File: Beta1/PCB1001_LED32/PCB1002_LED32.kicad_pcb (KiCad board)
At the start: 2 copper layers, 194 x 15.5 mm, 227 parts, among them U0 APA102C, U1 APA102C, U10 APA102C, U11 APA102C, U12 APA102C, U13 APA102C, U14 APA102C, U15 APA102C, U16 APA102C, U17 APA102C, U18 APA102C, U19 APA102C, U2 APA102C, U20 APA102C, U21 APA102C, U22 APA102C, U23 APA102C, U24 APA102C, U25 APA102C, U26 APA102C, U27 APA102C, U28 APA102C, U29 APA102C, U3 APA102C, U30 APA102C, U31 APA102C, U4 APA102C, U5 APA102C, U6 APA102C, U7 APA102C, U8 APA102C, U9 APA102C

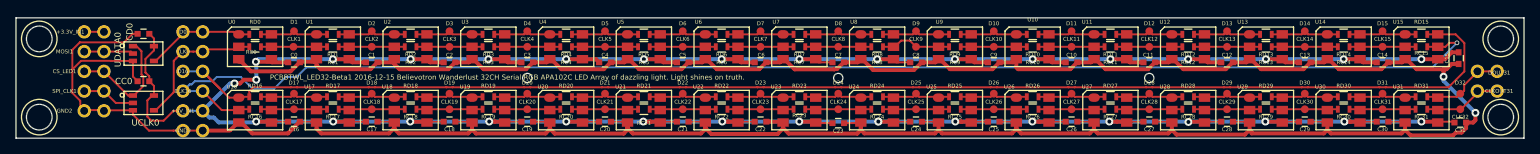
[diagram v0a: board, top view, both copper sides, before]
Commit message: Reduced width by 5.08, equally L/R
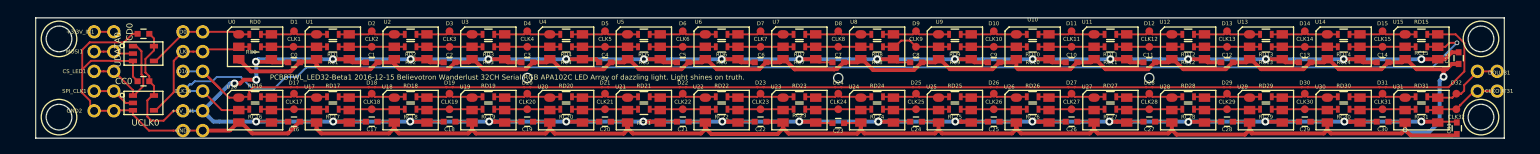
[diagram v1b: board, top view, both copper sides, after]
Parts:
- moved REF** 2.54 mm to (188.4, -12.8)
- moved REF** 2.54 mm to (188.4, -2.71)
- moved REF** 2.54 mm to (5.54, -12.8)
- moved REF** 2.54 mm to (5.54, -2.71)
- moved +3.3V_IN1 1.27 mm to (10.1, -13.7)
- moved CS_LED1 1.27 mm to (10.1, -8.60)
- moved GND2 1.27 mm to (10.1, -3.52)
- moved MOSI1 1.27 mm to (10.1, -11.1)
- moved SPI_CLK1 1.27 mm to (10.1, -6.06)
- moved +3.3V_INB1 1.27 mm to (12.6, -13.7)
- moved CS_LEDB1 1.27 mm to (12.6, -8.60)
- moved GNDB2 1.27 mm to (12.6, -3.52)
- moved MOSIB1 1.27 mm to (12.6, -11.1)
- moved SPI_CLKB1 1.27 mm to (12.6, -6.06)
- moved C31 0.87 mm to (185.3, -1.27), turned to 270 degrees
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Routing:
- net GND: track 456.4 -> 453.0 mm
- net Net-(SPI_CLK1-Pad1): track 6.90 -> 5.63 mm
- net Net-(MOSI1-Pad1): track 6.38 -> 5.11 mm
- net Net-(CS_LED1-Pad1): track 15.4 -> 14.5 mm
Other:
- board size 194 x 15.5 mm -> 188.9 x 15.5 mm

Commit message: Removed jumper resistors, b/c as they cause shorts.
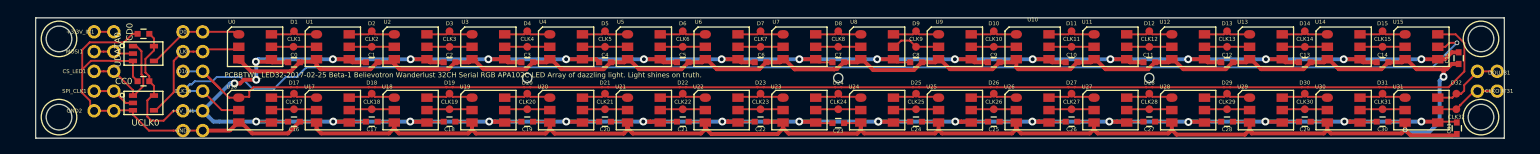
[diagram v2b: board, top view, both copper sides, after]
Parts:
- removed RC0, RC1, RC10, RC11, RC12, RC13, RC14, RC15, RC16, RC17, RC18, RC19, RC2, RC20, RC21, RC22, RC23, RC24, RC25, RC26, RC27, RC28, RC29, RC3, RC30, RC31, RC4, RC5, RC6, RC7, RC8, RC9, RD0, RD1, RD10, RD11, RD12, RD13, RD14, RD15, RD16, RD17, RD18, RD19, RD2, RD20, RD21, RD22, RD23, RD24, RD25, RD26, RD27, RD28, RD29, RD3, RD30, RD31, RD4, RD5, RD6, RD7, RD8, RD9: ZERO, Resistors_SMD:R_0603
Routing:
- net /CLK16: track 181.2 -> 178.5 mm
- net Net-(D31-Pad1): track 8.83 -> 6.13 mm
- net Net-(D30-Pad1): track 8.83 -> 6.13 mm
- net Net-(D29-Pad1): track 8.83 -> 6.13 mm
- net Net-(D28-Pad1): track 8.83 -> 6.13 mm
- net Net-(D27-Pad1): track 8.83 -> 6.13 mm
- net Net-(D15-Pad1): track 8.83 -> 6.13 mm
- net Net-(D14-Pad1): track 8.83 -> 6.13 mm
- net Net-(D13-Pad1): track 8.83 -> 6.13 mm
- net Net-(D11-Pad1): track 8.83 -> 6.13 mm
- net Net-(CLK31-Pad1): track 8.50 -> 5.80 mm
- net Net-(CLK30-Pad1): track 8.50 -> 5.80 mm
- net Net-(CLK29-Pad1): track 8.50 -> 5.80 mm
- net Net-(CLK28-Pad1): track 8.50 -> 5.80 mm
- net Net-(CLK27-Pad1): track 8.50 -> 5.80 mm
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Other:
- board text added: "PCBBTWL_LED32-2017-02-25 Beta-1 Believotron Wanderlust 32CH Serial RGB APA102C LED Array of dazzling light. Light shines on truth."
- board text removed: "PCBBTWL_LED32-Beta1 2016-12-15 Believotron Wanderlust 32CH Serial RGB APA102C LED Array of dazzling light. Light shines on truth."

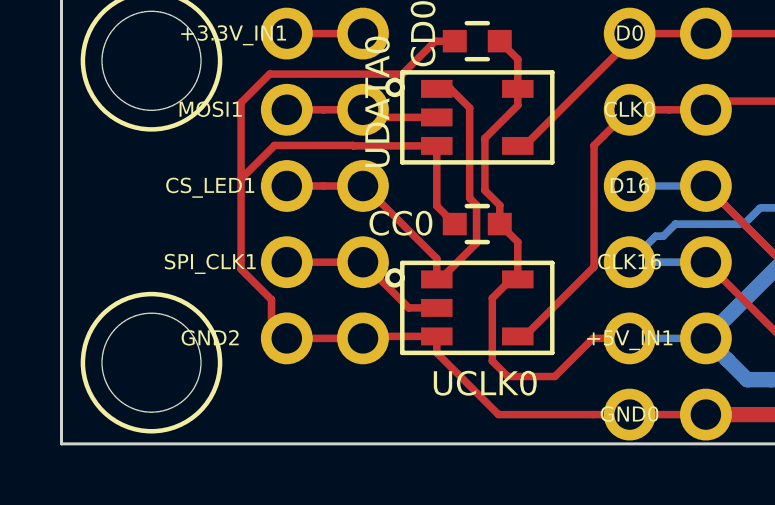
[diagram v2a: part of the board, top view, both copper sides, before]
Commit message: Added fiducial
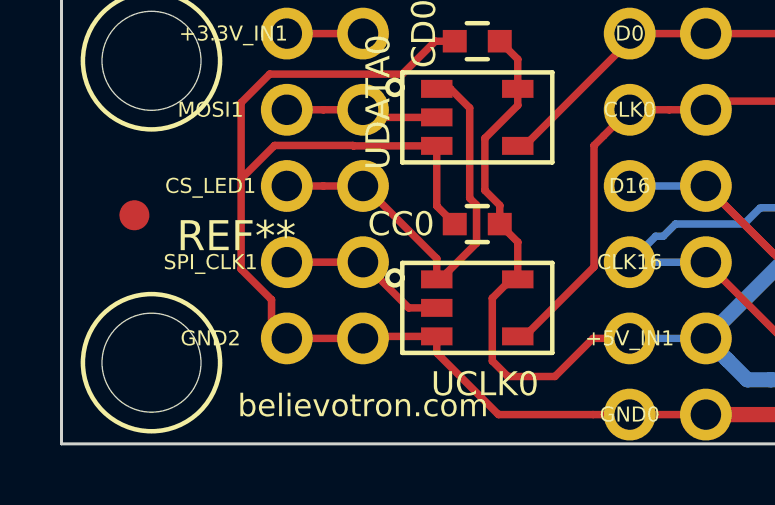
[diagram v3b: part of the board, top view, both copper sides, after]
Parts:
- added REF**: Fiducial_1mm_Dia_2.54mm_Outer_CopperTop, Fiducials:Fiducial_1mm_Dia_2.54mm_Outer_CopperTop, F.Cu at (4.97, -7.62)
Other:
- board text added: "believotron.com"
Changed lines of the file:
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@@
 (kicad_pcb (version 4) (host pcbnew 4.0.4-stable)
   (general
-    (links 286)
+    (links 0)
     (no_connects 0)
     (area 2.489999 -15.524901 191.470001 0.050001)
     (thickness 1.6)
-    (drawings 14)
+    (drawings 15)
     (tracks 786)
     (zones 0)
-    (modules 163)
+    (modules 164)
     (nets 73)
   )
@@
       (net 2 GND))
   )
+  (module Fiducials:Fiducial_1mm_Dia_2.54mm_Outer_CopperTop (layer F.Cu)
+    (at 4.97 -7.62)
+    (descr "Circular Fiducial, 1mm bare copper top; 2.54mm keepout")
+    (tags marker)
+    (attr virtual)
+    (fp_text reference REF** (at 3.4 0.7) (layer F.SilkS)
+      (effects (font (size 1 1) (thickness 0.15)))
+    )
+    (fp_text value Fiducial_1mm_Dia_2.54mm_Outer_CopperTop (at 0 -1.8) (layer F.Fab)
+      (effects (font (size 1 1) (thickness 0.15)))
+    )
+    (fp_circle (center 0 0) (end 1.55 0) (layer F.CrtYd) (width 0.05))
+    (pad ~ smd circle (at 0 0) (size 1 1) (layers F.Cu F.Mask)
+      (solder_mask_margin 0.77) (clearance 0.77))
+  )
+  (gr_text believotron.com (at 12.59 -1.27) (layer F.SilkS)
+    (effects (font (size 0.75 0.75) (thickness 0.1875)))
+  )
   (gr_text "PCBBTWL_LED32-2017-02-25 Beta-1 Believotron Wanderlust 32CH Serial RGB APA102C LED Array of dazzling light. Light shines on truth.\n" (at 26.814 -8.128) (layer F.SilkS)
